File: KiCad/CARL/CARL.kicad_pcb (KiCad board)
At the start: 2 copper layers, 168.2 x 111.7 mm, 46 parts, among them J1 Barrel_Jack (5V DC Supply), SW1 Beat_In_1, SW10 Power Switch, SW11 Mute_Button, SW12 Move_Left_Button, SW13 Move_Right_Button, SW14 Play_Button, SW2 Beat_In_2, SW3 Beat_In_3, SW4 Beat_In_4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

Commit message: PCB V2 and Schematic V3
-Updated schematic to utilize new voltage regulator setup.
-Updated PCB to reflect changes done in the schematic
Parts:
- added C10: 100nF, Capacitor_SMD:C_0805_2012Metric, F.Cu at (195.6, 92.9)
- added C3: 100nF, Capacitor_SMD:C_0805_2012Metric, F.Cu at (214.0, 95.0)
- added C4: 100nF, Capacitor_SMD:C_0805_2012Metric, F.Cu at (229.0, 95.0)
- added C5: 100nF, Capacitor_SMD:C_0805_2012Metric, F.Cu at (262.0, 93.0)
- added C6: 100nF, Capacitor_SMD:C_0805_2012Metric, F.Cu at (247.0, 93.0)
- added C7: 100nf, Capacitor_SMD:C_0805_2012Metric, F.Cu at (266.0, 93.0)
- added C8: 100nF, Capacitor_SMD:C_0805_2012Metric, F.Cu at (281.0, 93.0)
- added C9: 100nF, Capacitor_SMD:C_0805_2012Metric, F.Cu at (210.0, 93.0)
- added U6: LD1117V33 (3.3V Voltage Regulator), Package_TO_SOT_THT:TO-220-3_Vertical, F.Cu at (187.1, 107.0)
- added U7: L7805 (5V Voltage Regulator), Package_TO_SOT_THT:TO-220-3_Vertical, F.Cu at (257.0, 92.0)
- added U8: LD1117V33 (3.3V Voltage Regulator), Package_TO_SOT_THT:TO-220-3_Vertical, F.Cu at (276.0, 92.0)
- added U9: L7805 (5V Voltage Regulator), Package_TO_SOT_THT:TO-220-3_Vertical, F.Cu at (205.5, 92.0)
- C1: value 330nF -> 100nf
- J1: value Barrel_Jack (5V DC Supply) -> Barrel_Jack (9V DC Supply)
- RV2: value Gain_Control -> Gain_Control (10k POT); footprint Potentiometer_THT:Potentiometer_Bourns_3009Y_Horizontal -> Potentiometer_SMD:Potentiometer_ACP_CA6-VSMD_Vertical
- U2: value MIC5365-3.3YC5 (5V to 3.3V regulator) -> L7805 (5V Voltage Regulator); footprint Package_TO_SOT_SMD:SOT-353_SC-70-5 -> Package_TO_SOT_THT:TO-220-3_Vertical
- moved U2 40.6 mm to (218.9, 94.0)
- moved C2 17.8 mm to (192.0, 108.0), turned to 90 degrees
- moved C1 15.4 mm to (177.0, 108.0)
- moved RV2 7.46 mm to (247.0, 144.0)
- moved R17 2.99 mm to (204.4, 151.8)
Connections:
- A1 pad 2: 3.3V -> unconnected-(A1-3V3-Pad2)
- A1 pad 26: unconnected-(A1-USB-Pad26) -> 5V -ESP32 Power
- C1 pad 1: 5V -> Net-(SW10-B)
- C2 pad 1: 3.3V -> 3.3V -LCD Power
- D1 pad 2: 5V -> 5V -LED Driver Power
- D10 pad 2: 5V -> 5V -LED Driver Power
- D11 pad 2: 5V -> 5V -LED Driver Power
- D12 pad 2: 5V -> 5V -LED Driver Power
- D13 pad 2: 5V -> 5V -LED Driver Power
- D14 pad 2: 5V -> 5V -LED Driver Power
- D15 pad 2: 5V -> 5V -LED Driver Power
- D16 pad 2: 5V -> 5V -LED Driver Power
- D17 pad 2: 5V -> 5V -LED Driver Power
- D18 pad 2: 5V -> 5V -LED Driver Power
- D19 pad 2: 5V -> 5V -LED Driver Power
- D2 pad 2: 5V -> 5V -LED Driver Power
- D3 pad 2: 5V -> 5V -LED Driver Power
- D4 pad 2: 5V -> 5V -LED Driver Power
- D5 pad 2: 5V -> 5V -LED Driver Power
- D6 pad 2: 5V -> 5V -LED Driver Power
- D7 pad 2: 5V -> 5V -LED Driver Power
- D8 pad 2: 5V -> 5V -LED Driver Power
- D9 pad 2: 5V -> 5V -LED Driver Power
- R18 pad 2: 5V -> 5V -Amplifier Power
- RV2 pad 1: 5V -> 5V -Amplifier Power
- SW10 pad 2: 5V -> Net-(SW10-B)
- U1 pad 15: 3.3V -> 3.3V -LCD Power
- U1 pad 2: 3.3V -> 3.3V -LCD Power
- U2 pad 1: 5V -> Net-(SW10-B)
- U2 pad 3: 5V -> 5V -ESP32 Power
- U3 pad 7: 5V -> 5V -Amplifier Power
- U3 pad 8: 5V -> 5V -Amplifier Power
- U4 pad 32: 5V -> 5V -LED Driver Power
- U5 pad 17: 3.3V -> 3.3V -GPIO Extender Power
- U5 pad 9: 3.3V -> 3.3V -GPIO Extender Power
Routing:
- net 5V: track 372.9 -> 0.00 mm, vias 4 -> 0
- net 5V -LED Driver Power: track 0.00 -> 350.5 mm, vias 0 -> 6
- net 3.3V: track 177.5 -> 0.00 mm, vias 5 -> 0
- net Net-(SW10-B): track 0.00 -> 175.8 mm, vias 0 -> 2
- net 3.3V -GPIO Extender Power: track 0.00 -> 121.0 mm, vias 0 -> 6
- net Net-(A1-SDA/IO23): track 0.00 -> 120.0 mm, vias 0 -> 2
- net 3.3V -LCD Power: track 0.00 -> 115.6 mm, vias 0 -> 4
- net GND: track 4.65 -> 94.6 mm, vias 4 -> 7
- net Net-(A1-SCL/IO22): track 120.9 -> 193.1 mm, vias 9 -> 4
- net 5V -Amplifier Power: track 0.00 -> 70.9 mm, vias 0 -> 2
- net Net-(A1-MOSI/IO18): track 211.2 -> 141.4 mm
- net Net-(A1-SCK/IO5): track 210.6 -> 141.6 mm
- net 5V -ESP32 Power: track 0.00 -> 61.6 mm, vias 0 -> 2
- net Net-(D1-K): track 90.7 -> 134.8 mm, vias 0 -> 4
- net Net-(D2-K): track 69.4 -> 112.7 mm, vias 0 -> 4
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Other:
- board size 168.2 x 111.7 mm -> 168.2 x 112.9 mm

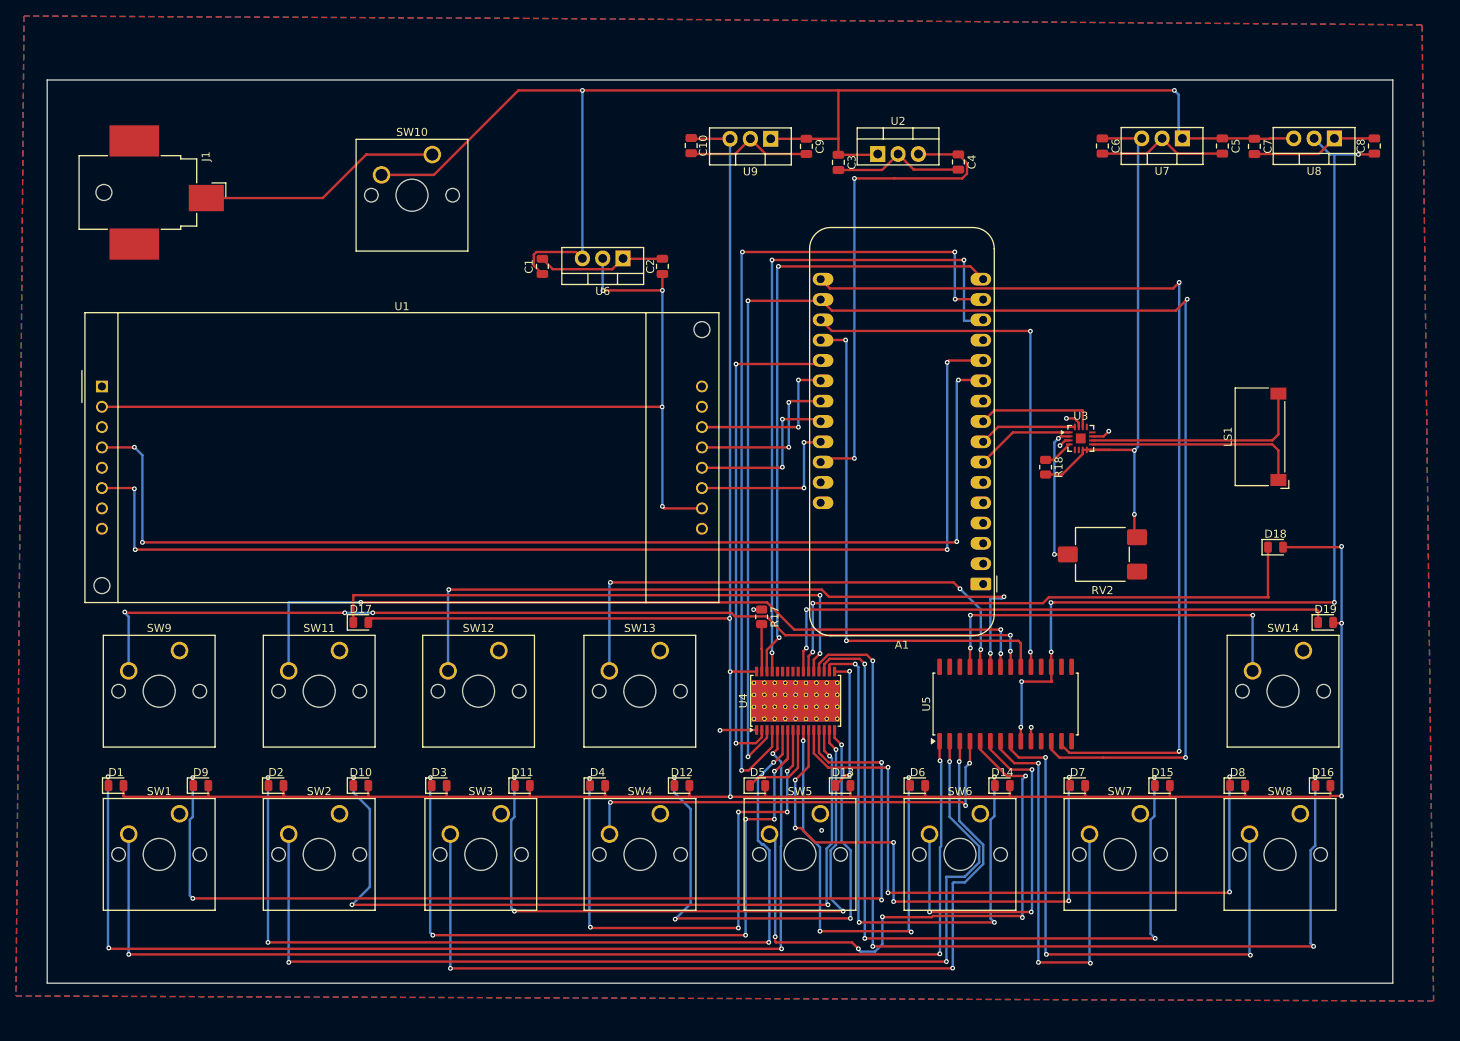
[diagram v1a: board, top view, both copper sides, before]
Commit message: Final Schematic and PCB
-Added test points  and 0 ohm resistors to the schematic.
-Added pullup resistors to I2C line
-Updated PCB and redid layout according to updated schematic.
-LED footprint updated to typical through hole PCB.
-Generated Gerbur Files
-Added Mounting Holes and Silkscreen
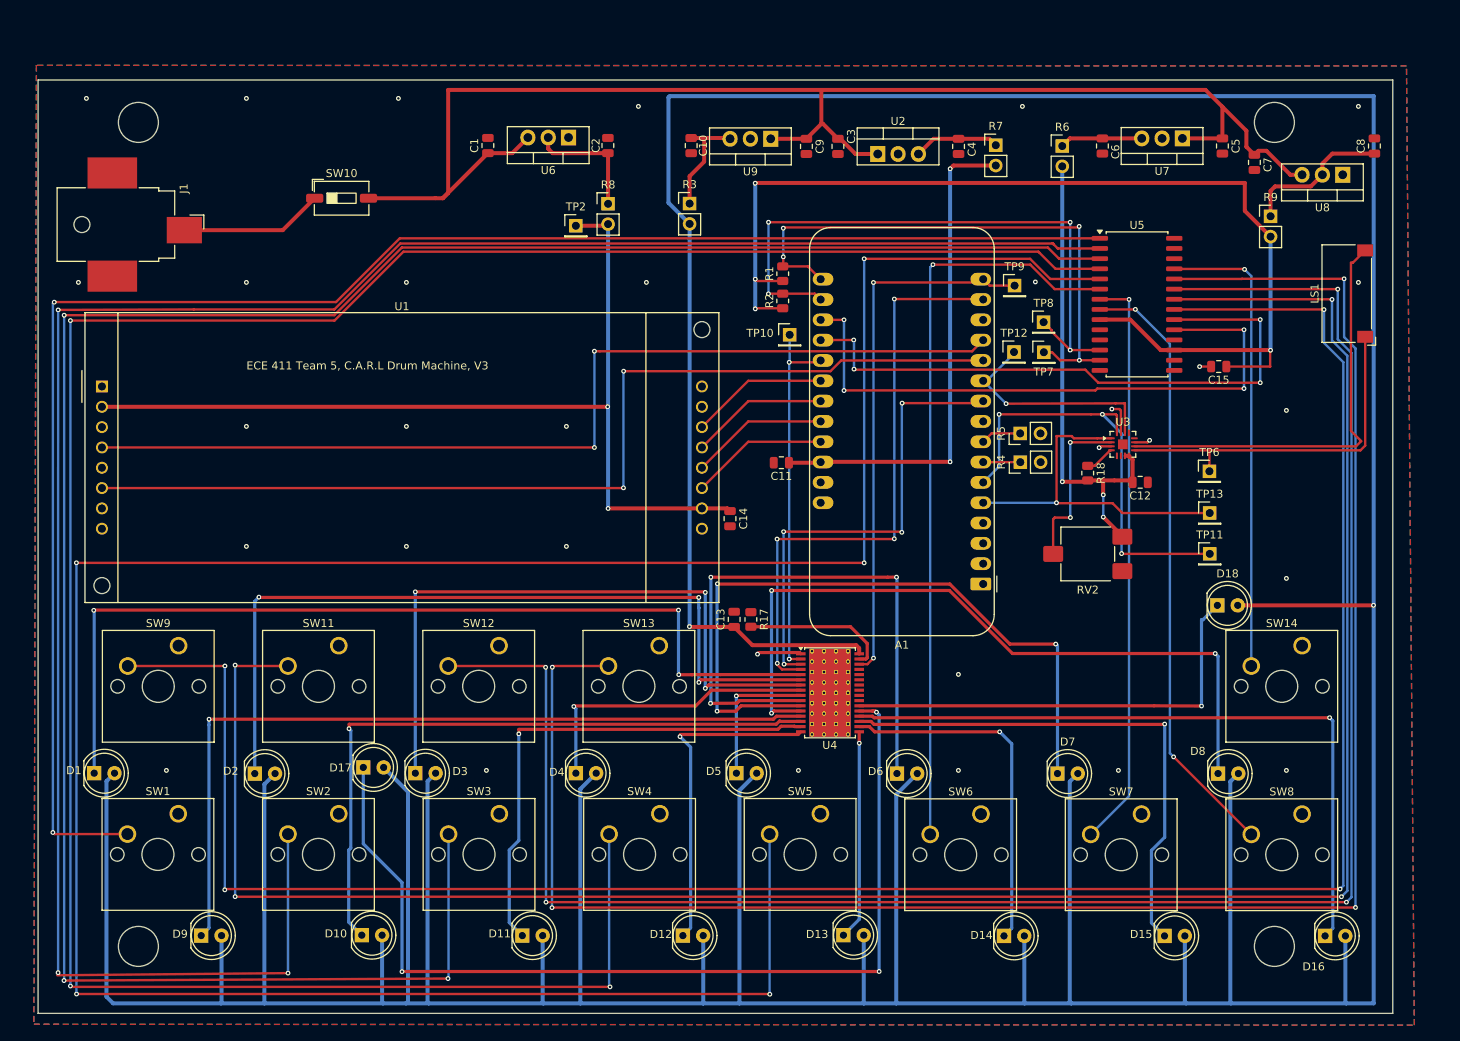
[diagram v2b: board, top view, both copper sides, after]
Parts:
- removed D19: LED_ORANGE, LED_SMD:LED_0805_2012Metric
- added C11: 100uf, Capacitor_SMD:C_0805_2012Metric, F.Cu at (206.9, 132.5)
- added C12: 100uf, Capacitor_SMD:C_0805_2012Metric, F.Cu at (251.7, 135.0)
- added C13: 100uf, Capacitor_SMD:C_0805_2012Metric, F.Cu at (201.0, 152.1)
- added C14: 100uf, Capacitor_SMD:C_0805_2012Metric, F.Cu at (200.4, 139.5)
- added C15: 100uf, Capacitor_SMD:C_0805_2012Metric, F.Cu at (261.5, 120.5)
- added R1: 4.7Kohm, Resistor_SMD:R_0805_2012Metric, F.Cu at (207.0, 108.9)
- added R2: 4.7Kohm, Resistor_SMD:R_0805_2012Metric, F.Cu at (207.0, 112.3)
- added R3: 0ohm, Connector_PinHeader_2.54mm:PinHeader_1x02_P2.54mm_Vertical, F.Cu at (195.4, 100.1)
- added R4: 0ohm, Connector_PinHeader_2.54mm:PinHeader_1x02_P2.54mm_Vertical, F.Cu at (236.7, 132.5)
- added R5: 0ohm, Connector_PinHeader_2.54mm:PinHeader_1x02_P2.54mm_Vertical, F.Cu at (236.7, 128.9)
- added R6: 0ohm, Connector_PinHeader_2.54mm:PinHeader_1x02_P2.54mm_Vertical, F.Cu at (242.0, 93.0)
- added R7: 0ohm, Connector_PinHeader_2.54mm:PinHeader_1x02_P2.54mm_Vertical, F.Cu at (233.7, 92.8)
- added R8: 0ohm, Connector_PinHeader_2.54mm:PinHeader_1x02_P2.54mm_Vertical, F.Cu at (185.2, 100.2)
- added R9: 0ohm, Connector_PinHeader_2.54mm:PinHeader_1x02_P2.54mm_Vertical, F.Cu at (268.0, 101.7)
- added TP10: TestPoint, Connector_PinHeader_2.54mm:PinHeader_1x01_P2.54mm_Vertical, F.Cu at (207.9, 116.5)
- added TP11: TestPoint, Connector_PinHeader_2.54mm:PinHeader_1x01_P2.54mm_Vertical, F.Cu at (260.4, 143.9)
- added TP12: TestPoint, Connector_PinHeader_2.54mm:PinHeader_1x01_P2.54mm_Vertical, F.Cu at (235.9, 118.7)
- added TP13: TestPoint, Connector_PinHeader_2.54mm:PinHeader_1x01_P2.54mm_Vertical, F.Cu at (260.4, 138.8)
- added TP2: TestPoint, Connector_PinHeader_2.54mm:PinHeader_1x01_P2.54mm_Vertical, F.Cu at (181.2, 102.9)
- added TP6: TestPoint, Connector_PinHeader_2.54mm:PinHeader_1x01_P2.54mm_Vertical, F.Cu at (260.4, 133.6)
- added TP7: TestPoint, Connector_PinHeader_2.54mm:PinHeader_1x01_P2.54mm_Vertical, F.Cu at (239.7, 118.7)
- added TP8: TestPoint, Connector_PinHeader_2.54mm:PinHeader_1x01_P2.54mm_Vertical, F.Cu at (239.7, 115.0)
- added TP9: TestPoint, Connector_PinHeader_2.54mm:PinHeader_1x01_P2.54mm_Vertical, F.Cu at (236.0, 110.4)
- D1, D10, D11, D12, D13, D14, D15, D16, D17, D18, D2, D3, D4, D5, D6, D7, D8, D9: footprint LED_SMD:LED_0805_2012Metric -> LED_THT:LED_D5.0mm
- SW10: footprint Button_Switch_Keyboard:SW_Cherry_MX_1.00u_PCB -> Button_Switch_SMD:SW_DIP_SPSTx01_Slide_6.7x4.1mm_W6.73mm_P2.54mm_LowProfile_JPin
- moved U5 52.6 mm to (251.3, 112.7), turned to 0 degrees
- moved LS1 20.9 mm to (277.6, 111.4)
- moved D16 18.8 mm to (274.8, 191.7)
- moved D15 18.8 mm to (254.8, 191.7)
- moved D14 18.8 mm to (234.7, 191.7)
- moved D12 18.8 mm to (194.6, 191.7)
- moved D9 18.8 mm to (134.4, 191.7)
- moved D11 18.8 mm to (174.5, 191.7)
- moved D10 18.7 mm to (154.4, 191.6)
- moved D13 18.7 mm to (214.6, 191.6)
- moved D17 18.1 mm to (154.6, 170.6)
- moved C1 16.6 mm to (170.2, 92.9)
- moved C2 16.6 mm to (185.2, 92.9)
- moved U6 16.6 mm to (180.3, 91.9)
- moved SW10 12.6 mm to (151.9, 99.5)
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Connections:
- A1 pad 10: unconnected-(A1-IO4/A5-Pad10) -> Net-(A1-IO4/A5)
- A1 pad 13: unconnected-(A1-MISO/IO19-Pad13) -> Net-(A1-MISO/IO19)
- A1 pad 14: Net-(A1-RX/IO16) -> unconnected-(A1-RX/IO16-Pad14)
- A1 pad 5: unconnected-(A1-DAC2/A0-Pad5) -> Net-(A1-DAC2/A0)
- A1 pad 6: unconnected-(A1-DAC1/A1-Pad6) -> Net-(A1-DAC1/A1)
- A1 pad 9: Net-(A1-IO36/A4) -> unconnected-(A1-IO36/A4-Pad9)
- C10 pad 1: 5V -LED Driver Power -> Net-(U9-OUT)
- C2 pad 1: 3.3V -LCD Power -> Net-(U6-VO)
- C4 pad 1: 5V -ESP32 Power -> Net-(U2-OUT)
- C6 pad 1: 5V -Amplifier Power -> Net-(U7-OUT)
- C8 pad 1: 3.3V -GPIO Extender Power -> Net-(U8-VO)
- U1 pad 4: Net-(A1-SCK/IO5) -> Net-(A1-MISO/IO19)
- U2 pad 3: 5V -ESP32 Power -> Net-(U2-OUT)
- U3 pad 1: Net-(A1-I34/A2) -> Net-(A1-DAC2/A0)
- U3 pad 14: Net-(A1-IO36/A4) -> Net-(A1-SCK/IO5)
- U3 pad 16: Net-(A1-I39/A3) -> Net-(A1-DAC1/A1)
- U4 pad 23: Net-(D19-K) -> unconnected-(U4-OUT18-Pad23)
- U4 pad 29: Net-(A1-RX/IO16) -> unconnected-(U4-SOUT-Pad29)
- U4 pad 3: Net-(A1-SCL/IO22) -> Net-(A1-IO4/A5)
- U6 pad 2: 3.3V -LCD Power -> Net-(U6-VO)
- U7 pad 3: 5V -Amplifier Power -> Net-(U7-OUT)
- U8 pad 2: 3.3V -GPIO Extender Power -> Net-(U8-VO)
- U9 pad 3: 5V -LED Driver Power -> Net-(U9-OUT)
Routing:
- net 5V -LED Driver Power: track 350.5 -> 800.7 mm, vias 6 -> 2
- net Net-(U5-GPB4): track 75.0 -> 327.7 mm
- net Net-(U5-GPB3): track 56.9 -> 303.0 mm
- net Net-(U5-GPA3): track 66.0 -> 238.0 mm, vias 3 -> 4
- net Net-(U5-GPB2): track 111.6 -> 282.8 mm
- net Net-(U5-GPA1): track 103.6 -> 269.4 mm, vias 3 -> 4
- net Net-(U5-GPA2): track 90.3 -> 239.8 mm, vias 3 -> 4
- net Net-(U5-GPA0): track 123.4 -> 271.9 mm, vias 5 -> 4
- net Net-(U5-GPB1): track 130.4 -> 263.2 mm
- net Net-(A1-MISO/IO19): track 0.00 -> 122.8 mm, vias 0 -> 2
- net Net-(A1-SCL/IO22): track 193.1 -> 78.1 mm
- net Net-(A1-SCK/IO5): track 141.6 -> 28.0 mm, vias 4 -> 1
- net Net-(A1-RX/IO16): track 85.5 -> 0.00 mm, vias 3 -> 0
- net GND: track 94.6 -> 14.5 mm, vias 7 -> 32
- net Net-(D19-K): track 73.4 -> 0.00 mm, vias 2 -> 0
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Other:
- board size 168.2 x 112.9 mm -> 169.3 x 116.7 mm
- board text added: "ECE 411 Team 5, C.A.R.L Drum Machine, V3"
